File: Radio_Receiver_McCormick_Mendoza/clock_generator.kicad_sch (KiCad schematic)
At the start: 13 parts, among them J10 CLK_2, J11 I_LO, J12 Q_LO, J24 CLK_0, J9 CLK_1, U5 Si5351A-B-GT, U6 74AC74, U7 74AC74, Y2 ASTX-H11-24.576MHZ-T

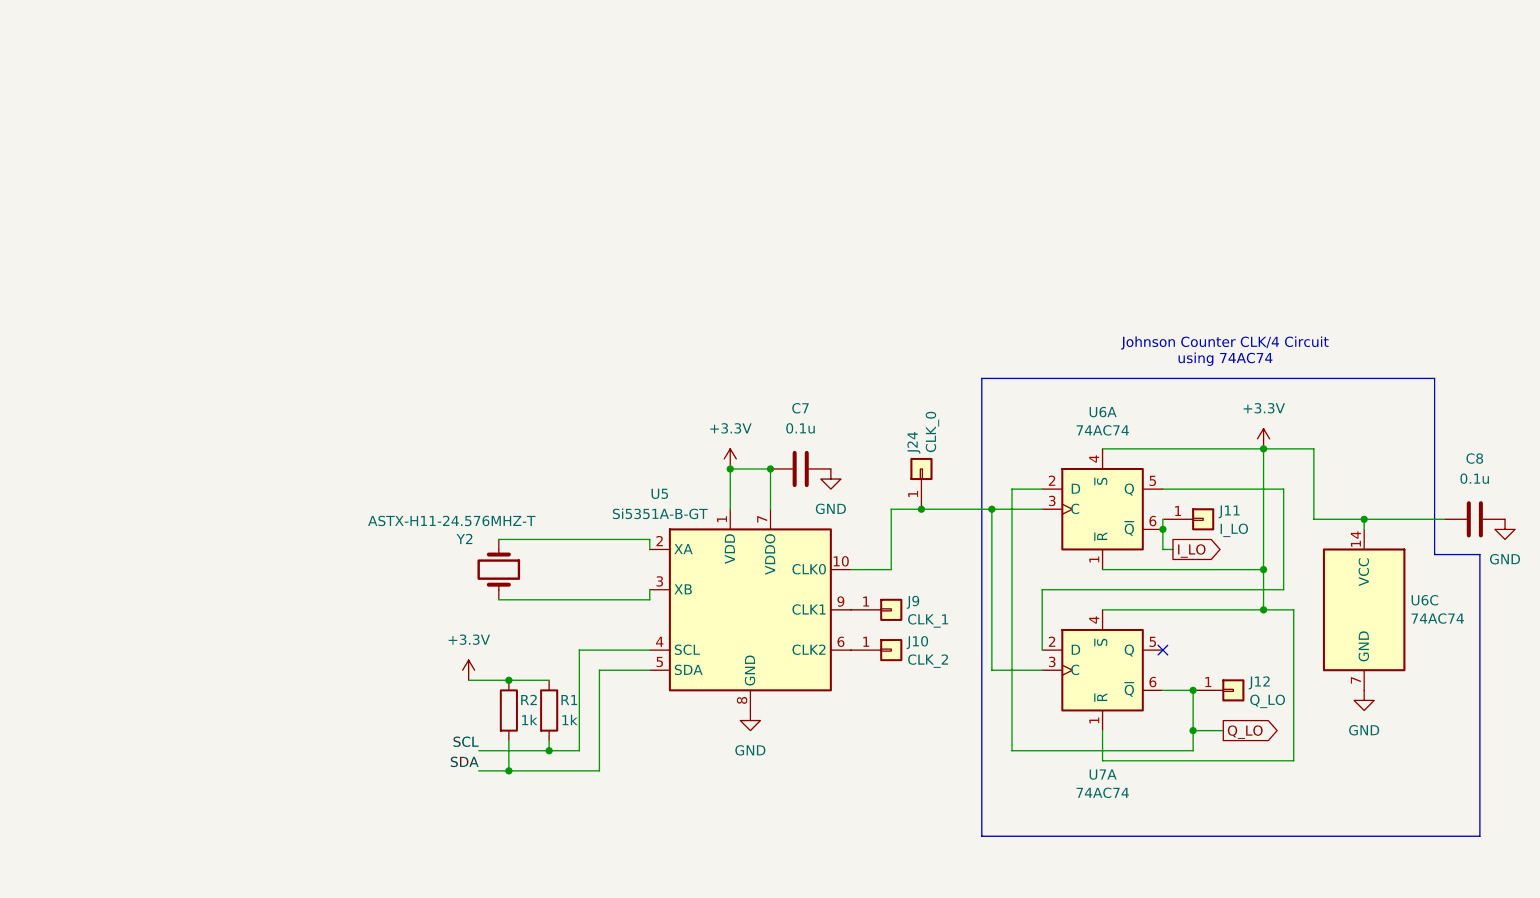
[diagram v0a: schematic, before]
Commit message: Added digital power regulator
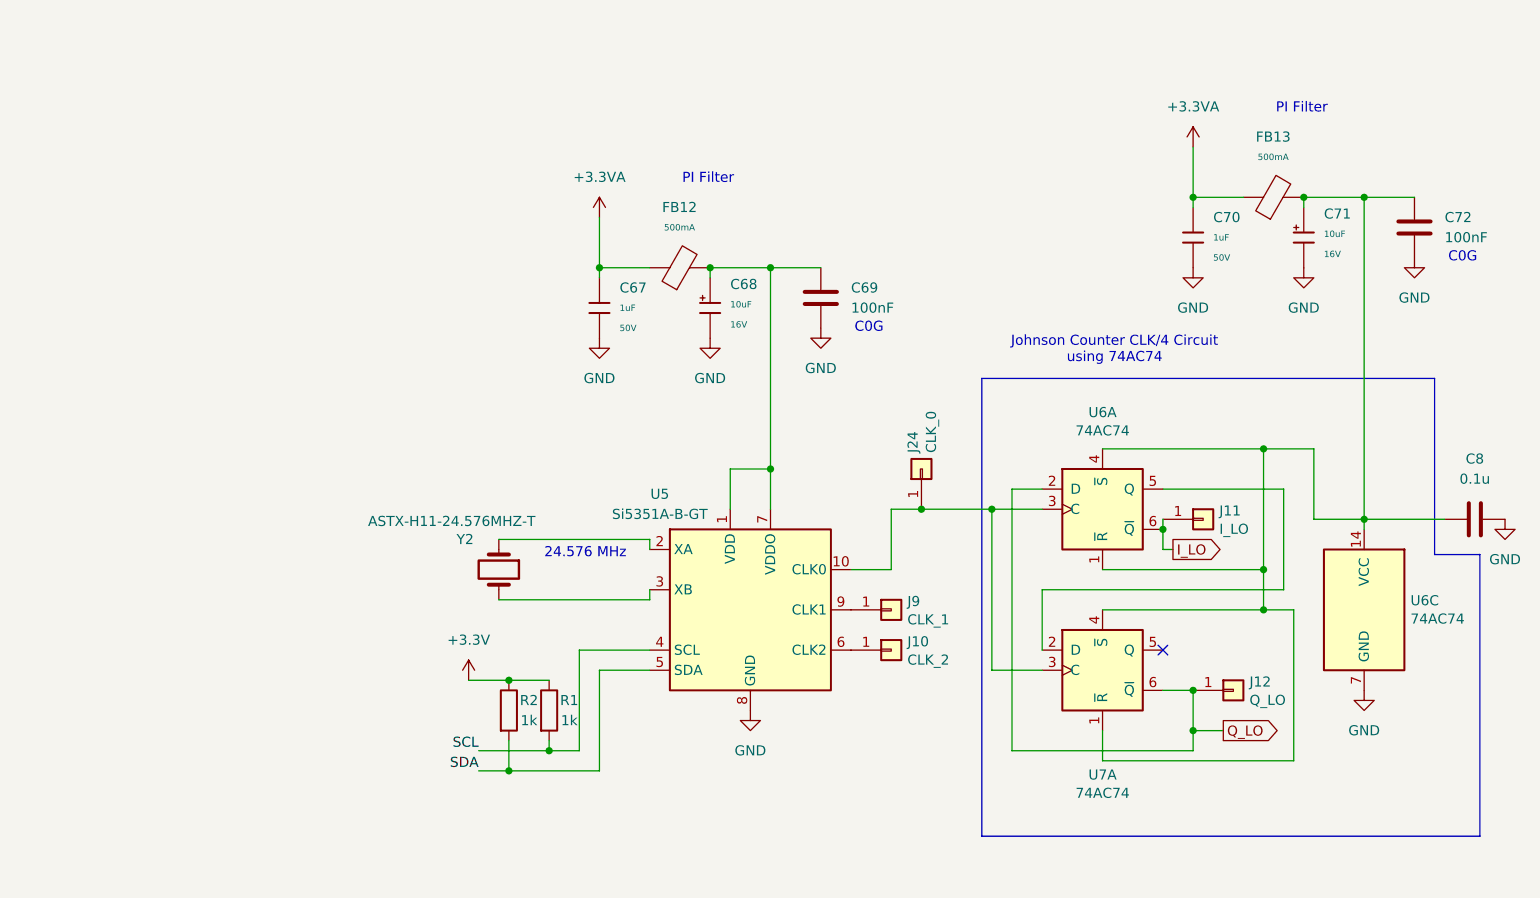
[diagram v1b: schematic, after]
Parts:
- removed C7: 0.1u, Capacitor_THT:C_Disc_D5.1mm_W3.2mm_P5.00mm, symbol Device:C
- added C67, C70: 1uF, PCM_JLCPCB:C_0603, symbol PCM_JLCPCB-Capacitors:0603,1uF
- added C68, C71: 10uF, PCM_JLCPCB:C_CASE-A-3216-18(mm), symbol PCM_JLCPCB-Capacitors:CASE-A-3216-18(mm),10uF
- added C69, C72: 100nF, PCM_JLCPCB:C_1206, symbol Device:C
- added FB12, FB13: (no value), PCM_JLCPCB:FB_0805, symbol PCM_JLCPCB-Inductors:Ferrite,0805,(2)
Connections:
- net +3.3V: no longer C8.1, U5.1 (VDD), U5.7 (VDDO), U6.1 (~{R}), U6.14 (VCC), U6.4 (~{S}), U7.1 (~{R}), U7.4 (~{S})
- net GND: now also C67.2, C68.2, C69.2, C70.2, C71.2, C72.2
- new net: C71.1, C72.1, C8.1, FB13.2, U6.1 (~{R}), U6.14 (VCC), U6.4 (~{S}), U7.1 (~{R}), U7.4 (~{S})
- new net: C68.1, C69.1, FB12.2, U5.1 (VDD), U5.7 (VDDO)
- new net +3.3VA: C67.1, C70.1, FB12.1, FB13.1
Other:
- note added: "24.576 MHz"
- note added: "C0G"
- note added: "PI Filter"

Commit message: Integrated signal path modules
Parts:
- removed C67: 1uF, PCM_JLCPCB:C_0603, symbol PCM_JLCPCB-Capacitors:0603,1uF
- removed C68: 10uF, PCM_JLCPCB:C_CASE-A-3216-18(mm), symbol PCM_JLCPCB-Capacitors:CASE-A-3216-18(mm),10uF
- removed C69: 100nF, PCM_JLCPCB:C_1206, symbol Device:C
- removed FB12: (no value), PCM_JLCPCB:FB_0805, symbol PCM_JLCPCB-Inductors:Ferrite,0805,(2)
- added C75: 1uF, PCM_JLCPCB:C_0603, symbol PCM_JLCPCB-Capacitors:0603,1uF
- added C76, C80: 10uF, PCM_JLCPCB:C_CASE-A-3216-18(mm), symbol PCM_JLCPCB-Capacitors:CASE-A-3216-18(mm),10uF
- added C77, C78: 100nF, PCM_JLCPCB:C_1206, symbol Device:C
- added FB15, FB16: (no value), PCM_JLCPCB:FB_0805, symbol PCM_JLCPCB-Inductors:Ferrite,0805,(2)
- added R4: 2.2Ω, PCM_JLCPCB:R_0805, symbol PCM_JLCPCB-Resistors:0805,2.2Ω
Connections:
- net +3.3VA: now also C75.1, FB15.1, R4.1
- net GND: now also C75.2, C76.2, C77.2, C78.2, C80.2
- net at U5.1 (VDD): now also C76.1, C77.1, FB15.2; no longer U5.7 (VDDO)
- new net: FB16.1, R4.2
- new net: C78.1, C80.1, FB16.2, U5.7 (VDDO)
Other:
- note added: "ASK FROHNE IF 3.3VA is better than 3.3V here"
- note added: "PI Filters"

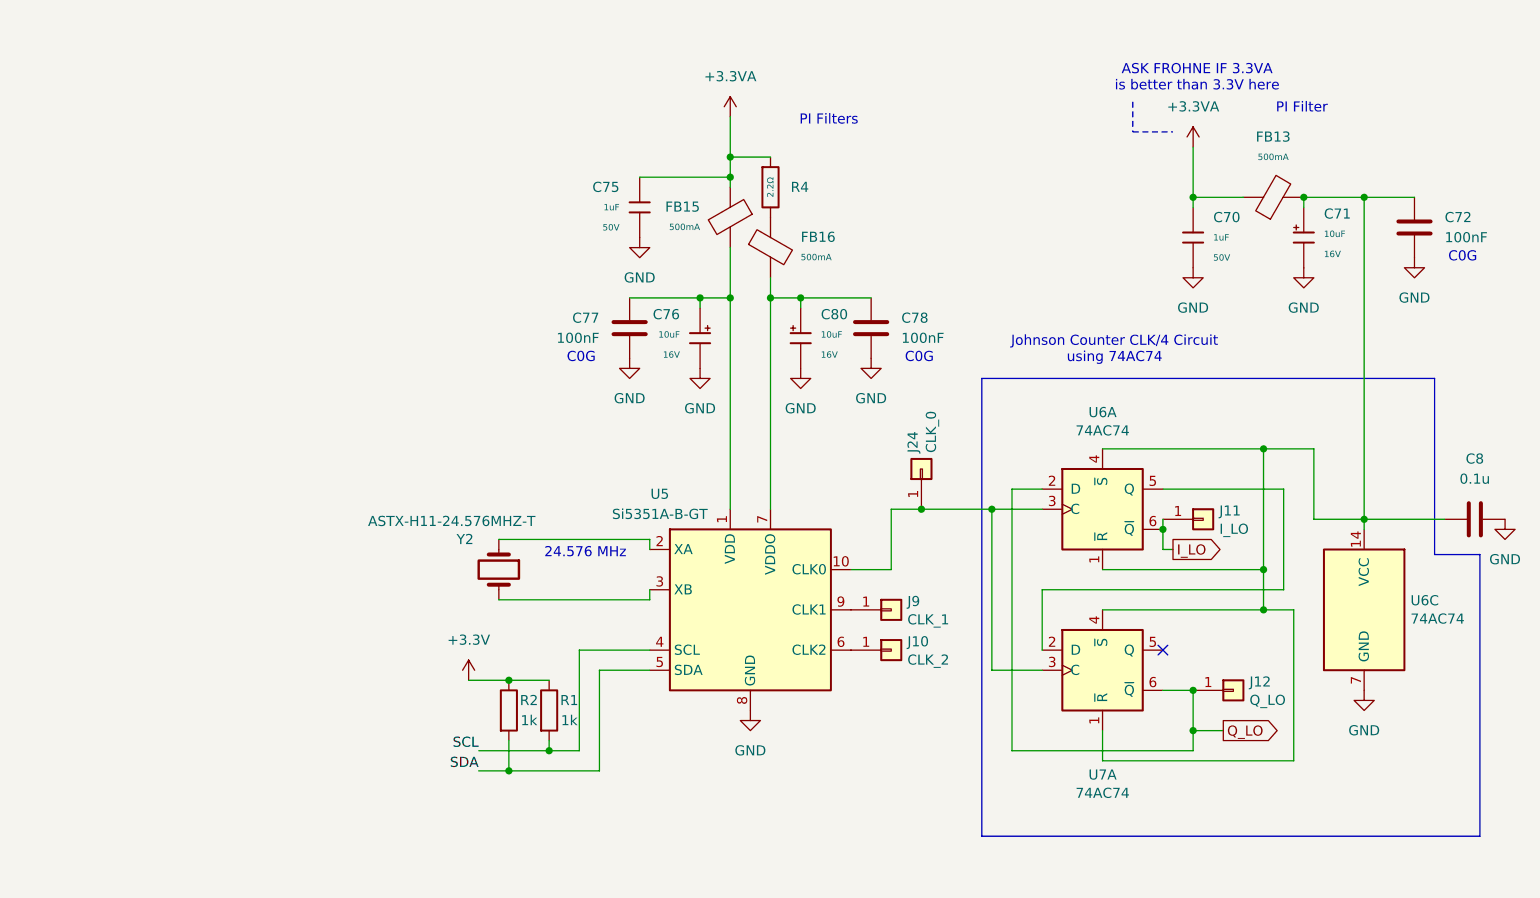
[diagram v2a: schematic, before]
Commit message: Finalized Pico connections and added indicator LEDs
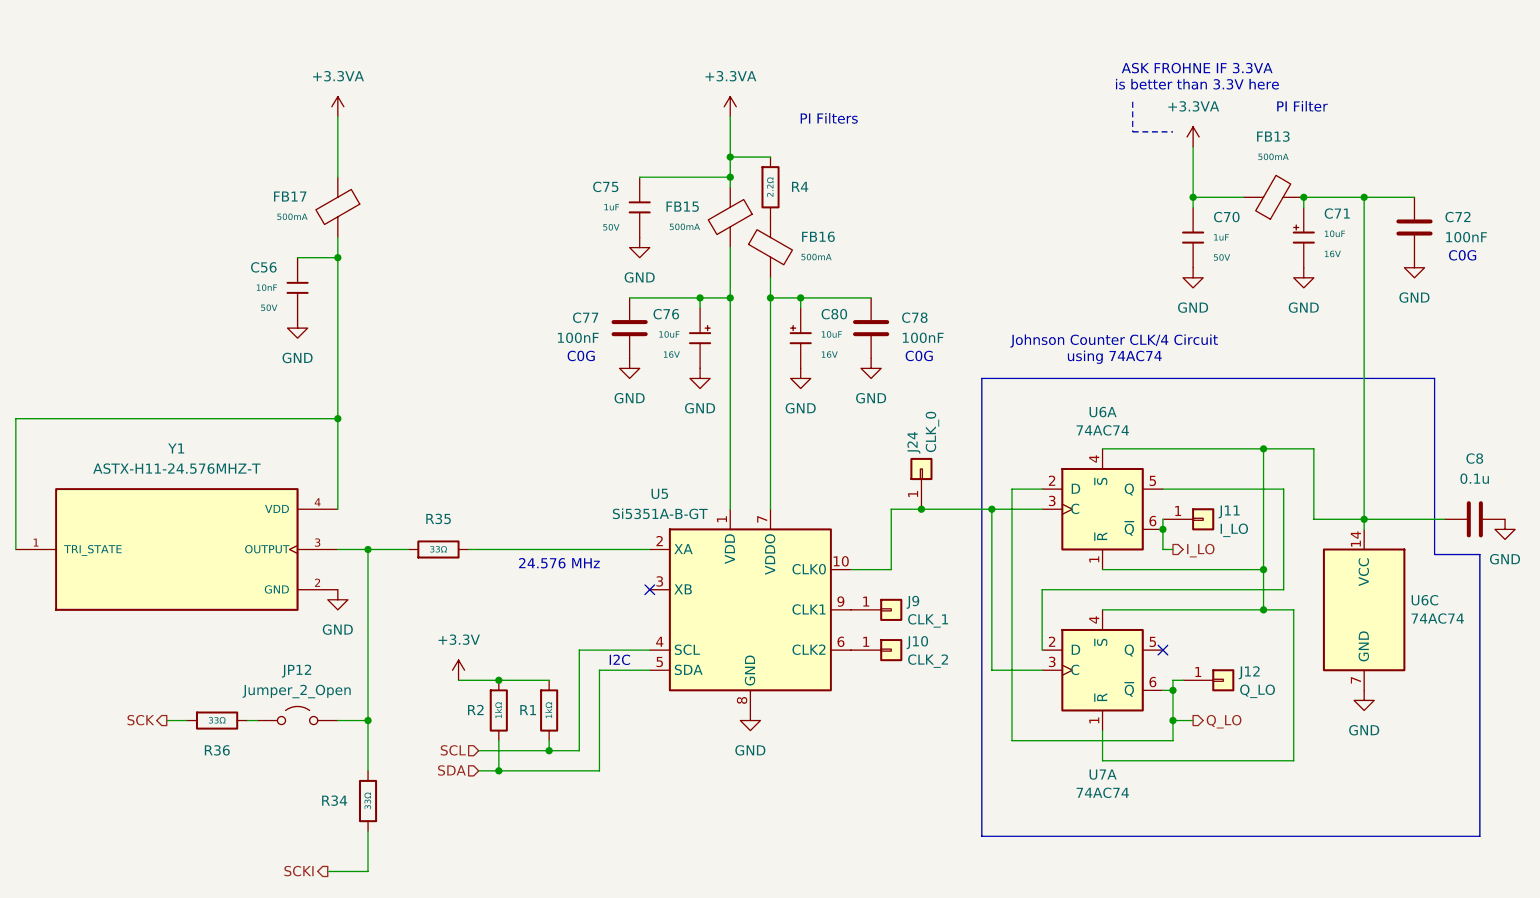
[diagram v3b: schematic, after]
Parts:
- removed R1, R2: 1k, symbol Device:R
- removed Y2: ASTX-H11-24.576MHZ-T, symbol Device:Crystal
- added C56: 10nF, PCM_JLCPCB:C_0805, symbol PCM_JLCPCB-Capacitors:0805,10nF
- added FB17: (no value), PCM_JLCPCB:FB_0805, symbol PCM_JLCPCB-Inductors:Ferrite,0805,(2)
- added JP12: Jumper_2_Open, symbol Jumper:Jumper_2_Open
- added R1, R2: 1kΩ, PCM_JLCPCB:R_0402, symbol PCM_JLCPCB-Resistors:0402,1kΩ
- added R34, R35, R36: 33Ω, PCM_JLCPCB:R_0805, symbol PCM_JLCPCB-Resistors:0805,33Ω
- added Y1: ASTX-H11-24.576MHZ-T, ASTX-H11-24.576MHZ-T:XTAL_ASTX-H11-24.576MHZ-T, symbol ASTX-H11-24.576MHZ-T:ASTX-H11-24.576MHZ-T
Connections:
- net +3.3V: now also R1.1, R2.1
- net +3.3VA: now also FB17.1
- net GND: now also C56.2, Y1.2 (GND)
- net SCL: now also R1.2
- net SDA: now also R2.2
- net at U5.2 (XA): now also R35.2
- new net: JP12.1 (A), R36.2
- new net: JP12.2 (B), R34.2, R35.1, Y1.3 (OUTPUT)
- new net: C56.1, FB17.2, Y1.1 (TRI_STATE), Y1.4 (VDD)
- new net SCK: R36.1
- new net SCKI: R34.1
- no-connect marks 1 -> 2
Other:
- note added: "I2C"
- moved on the sheet: J12

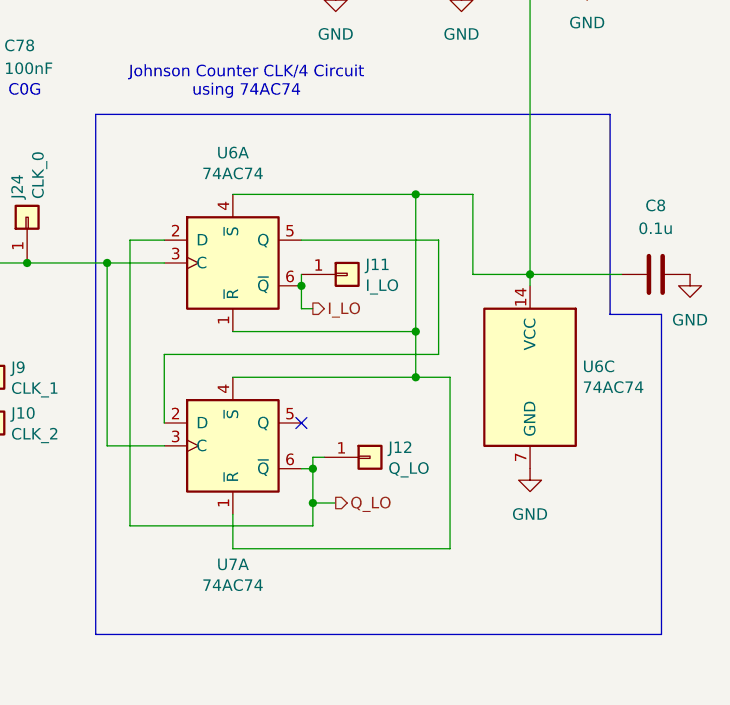
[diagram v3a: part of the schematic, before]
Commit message: Added transformer footprint and datasheet
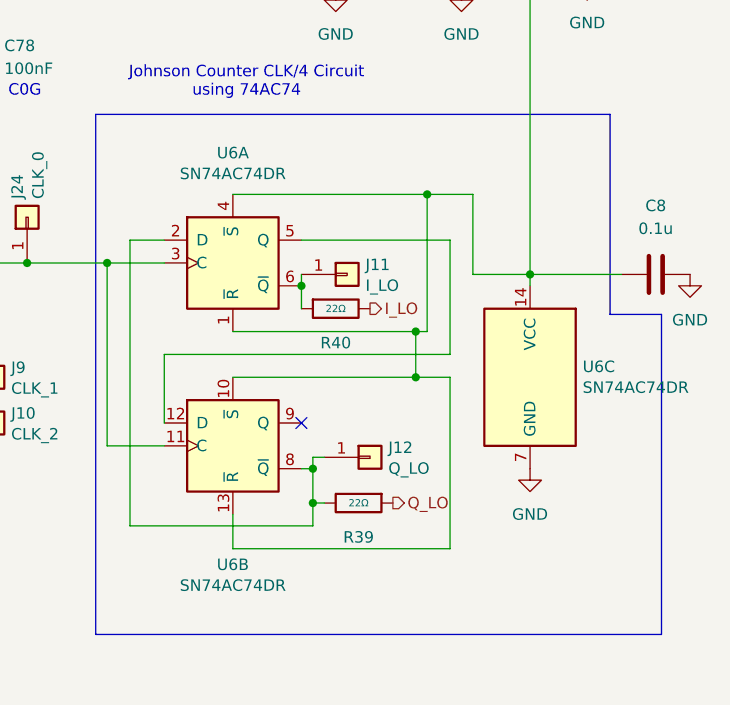
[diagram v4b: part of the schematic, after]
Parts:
- added R39, R40: 22Ω, PCM_JLCPCB:R_0603, symbol PCM_JLCPCB-Resistors:0603,22Ω
- C56, C70, C75: Manufacturer Samsung Electro-Mechanics -> (none)
- C71, C76, C80: Manufacturer AVX -> (none)
- FB13, FB15, FB16, FB17: Manufacturer Sunlord -> (none)
- R1, R2, R34, R35, R36, R4: Manufacturer UNI-ROYAL(Uniroyal Elec) -> (none)
- U5: LCSC (none) -> C504891; Price (none) -> 4.4539USD
- U6: value 74AC74 -> SN74AC74DR; footprint Package_DIP:DIP-14_W7.62mm -> SN74AC74DR:D14; LCSC (none) -> C352945; Price (none) -> 3.1779USD
- U6: renamed from U7; value 74AC74 -> SN74AC74DR; footprint Package_DIP:DIP-14_W7.62mm -> SN74AC74DR:D14; LCSC (none) -> C352945; Price (none) -> 3.1779USD
- Y1: LCSC (none) -> C1987701; Price (none) -> 11.0970 USD
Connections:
- net I_LO: now also R40.2; no longer J11.1 (Pin_1), U6.6 (~{Q})
- net Q_LO: now also R39.1; no longer J12.1 (Pin_1), U6.2 (D), U6.6 (~{Q})
- net at C71.1, C72.1, C8.1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: now also U6.10 (~{S}), U6.13 (~{R}); no longer U6.1 (~{R}), U6.4 (~{S})
- net at J24.1 (Pin_1), U5.10 (CLK0), U6.3 (C): now also U6.11 (C); no longer U6.3 (C)
- net at U6.5 (Q): now also U6.12 (D); no longer U6.2 (D)
- new net: J12.1 (Pin_1), R39.2, U6.2 (D), U6.8 (~{Q})
- new net: J11.1 (Pin_1), R40.1, U6.6 (~{Q})

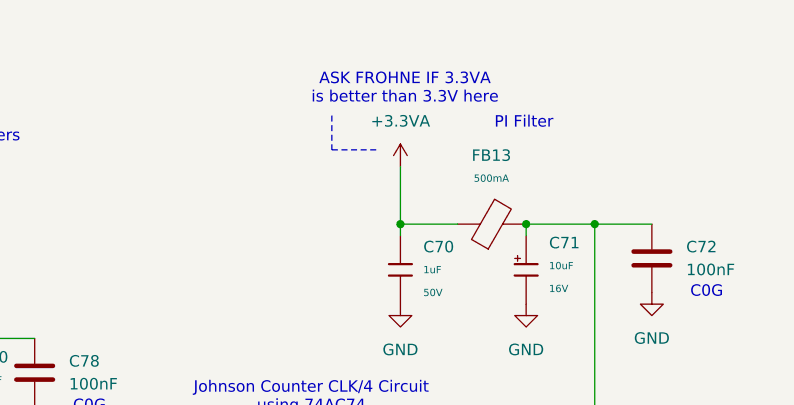
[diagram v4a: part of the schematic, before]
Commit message: Swapped voltage regulator to output 4.5V
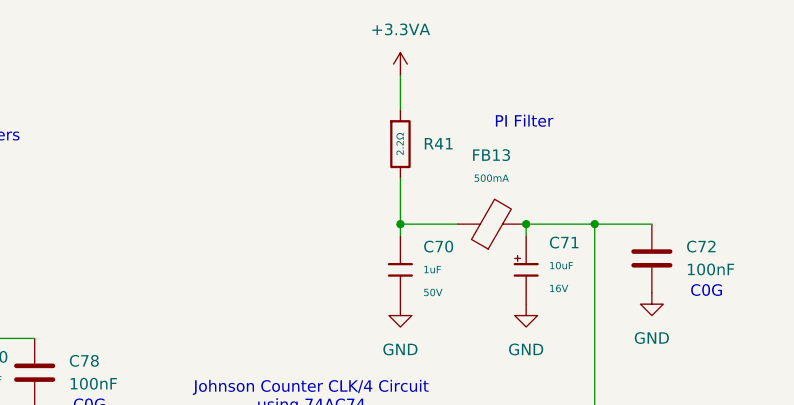
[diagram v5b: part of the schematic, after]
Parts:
- added R41: 2.2Ω, PCM_JLCPCB:R_0805, symbol PCM_JLCPCB-Resistors:0805,2.2Ω
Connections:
- net +3.3VA: now also R41.1; no longer C70.1, FB13.1
- new net: C70.1, FB13.1, R41.2
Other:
- note removed: "ASK FROHNE IF 3.3VA is better than 3.3V here"
